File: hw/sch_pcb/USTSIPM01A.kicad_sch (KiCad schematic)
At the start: 41 parts, among them J4 HEADER_2x01_PARALLEL, J5 HEADER_2x01_PARALLEL, J6 HEADER_2x01_PARALLEL, J8 HEADER_2x01_PARALLEL, J9 HEADER_2x01_PARALLEL, M1 HOLE, M2 HOLE, M3 HOLE, M4 HOLE, U1 MICROFC-60035-SMT-TR(1), U2 OPA836IDB

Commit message: Edit schema
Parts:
- removed C1: 15uF/35V, Mlab_C:TantalC_SizeC_Reflow, symbol AIRDOSC01A_PCB01A-rescue:CP-Device
- added C1: 10uF/35V, Capacitor_SMD:C_0805_2012Metric, symbol Device:C
- C10, C11, C12, C13, C2: renamed from C?; footprint Mlab_R:SMD-0805 -> Capacitor_SMD:C_0805_2012Metric
- C3: UST_ID 5c70984412875079b91f8867 -> (none)
- C4, C7: value 10u -> 10uF; footprint Mlab_R:SMD-0805 -> Capacitor_SMD:C_0805_2012Metric; UST_ID 5c70984712875079b91f8b53 -> (none)
- C5, C6, C8, C9: footprint Mlab_R:SMD-0805 -> Capacitor_SMD:C_0805_2012Metric
- gave numbers to parts that had none: 6
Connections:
- net GND: now also C1.2
- net at R1.1, R2.2: now also C1.1
- net #PD: no longer names the net of R11.2, U2.5 (~{DIS})

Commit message: Editing schema and PCB
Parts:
- removed C3: 47uF, Mlab_C:TantalC_SizeC_Reflow, symbol AIRDOSC01A_PCB01A-rescue:CP-Device
- removed D1: M4, Mlab_D:Diode-SMA_Standard, symbol Device:D
- added C14, C15, C3: 10uF, Capacitor_SMD:C_0805_2012Metric, symbol Device:C
- added D1: BZX585-B5V6.115, Diode_SMD:D_SOD-523, symbol MLAB_D:D_ZENER
- L1: value 400uH cca 0,9mA -> 400uH cca 0,9mA NLV10JT391; footprint (none) -> Inductor_SMD:L_1210_3225Metric_Pad1.42x2.65mm_HandSolder
- R1, R10, R11, R12, R13, R2, R3, R4, R5, R6, R7, R8, R9: footprint Mlab_R:SMD-0805 -> Resistor_SMD:R_0805_2012Metric
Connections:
- net +3V6: now also C14.1, C15.1, C3.1, D1.1 (K)
- net GND: now also C14.2, C15.2, C3.2, D1.2 (A)
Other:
- moved on the sheet: C4, C7, C8, R3

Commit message: Editing PCB
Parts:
- removed M1, M2, M3, M4: HOLE, Mlab_Mechanical:MountingHole_3mm, symbol MLAB_MECHANICAL:HOLE
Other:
- note removed: "MOUNTING HOLES"
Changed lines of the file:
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@@
   (junction (at 121.412 127.508) (diameter 1.016) (color 0 0 0 0)
   )
-  (junction (at 269.24 15.24) (diameter 1.016) (color 0 0 0 0)
-  )
   (junction (at 60.452 100.838) (diameter 1.016) (color 0 0 0 0)
   )
-  (junction (at 264.16 15.24) (diameter 1.016) (color 0 0 0 0)
-  )
   (junction (at 144.78 53.848) (diameter 0) (color 0 0 0 0)
   )
@@
   )
   (junction (at 71.882 100.838) (diameter 1.016) (color 0 0 0 0)
-  )
-  (junction (at 274.32 15.24) (diameter 1.016) (color 0 0 0 0)
   )
   (no_connect (at 103.632 113.538))
@@
     (stroke (width 0) (type default) (color 0 0 0 0))
   )
-  (wire (pts (xy 279.4 15.24) (xy 279.4 16.51))
-    (stroke (width 0) (type solid) (color 0 0 0 0))
-  )
-  (wire (pts (xy 274.32 15.24) (xy 279.4 15.24))
-    (stroke (width 0) (type solid) (color 0 0 0 0))
-  )
-  (polyline (pts (xy 246.38 13.97) (xy 246.38 24.13))
-    (stroke (width 0) (type dash) (color 0 0 0 0))
-  )
   (wire (pts (xy 85.852 178.562) (xy 78.232 178.562))
     (stroke (width 0) (type solid) (color 0 0 0 0))
@@
     (stroke (width 0) (type solid) (color 0 0 0 0))
   )
-  (wire (pts (xy 269.24 15.24) (xy 274.32 15.24))
-    (stroke (width 0) (type solid) (color 0 0 0 0))
-  )
   (wire (pts (xy 144.272 147.828) (xy 155.702 147.828))
     (stroke (width 0) (type solid) (color 0 0 0 0))
@@
     (stroke (width 0) (type solid) (color 0 0 0 0))
   )
-  (polyline (pts (xy 281.94 13.97) (xy 281.94 24.13))
-    (stroke (width 0) (type dash) (color 0 0 0 0))
-  )
   (wire (pts (xy 60.452 112.268) (xy 60.452 110.998))
     (stroke (width 0) (type solid) (color 0 0 0 0))
@@
     (stroke (width 0) (type default) (color 0 0 0 0))
   )
-  (polyline (pts (xy 246.38 13.97) (xy 281.94 13.97))
-    (stroke (width 0) (type dash) (color 0 0 0 0))
-  )
-  (wire (pts (xy 264.16 15.24) (xy 269.24 15.24))
-    (stroke (width 0) (type solid) (color 0 0 0 0))
-  )
   (wire (pts (xy 46.482 100.838) (xy 49.022 100.838))
     (stroke (width 0) (type solid) (color 0 0 0 0))
   )
-  (wire (pts (xy 274.32 16.51) (xy 274.32 15.24))
-    (stroke (width 0) (type solid) (color 0 0 0 0))
-  )
   (wire (pts (xy 58.166 178.562) (xy 68.072 178.562))
     (stroke (width 0) (type solid) (color 0 0 0 0))
   )
-  (wire (pts (xy 259.08 16.51) (xy 259.08 15.24))
-    (stroke (width 0) (type solid) (color 0 0 0 0))
-  )
   (wire (pts (xy 144.78 64.008) (xy 148.59 64.008))
     (stroke (width 0) (type default) (color 0 0 0 0))
@@
     (stroke (width 0) (type solid) (color 0 0 0 0))
   )
-  (polyline (pts (xy 246.38 24.13) (xy 281.94 24.13))
-    (stroke (width 0) (type dash) (color 0 0 0 0))
-  )
   (wire (pts (xy 238.76 66.548) (xy 238.76 64.008))
     (stroke (width 0) (type default) (color 0 0 0 0))
@@
     (stroke (width 0) (type default) (color 0 0 0 0))
   )
-  (wire (pts (xy 259.08 15.24) (xy 264.16 15.24))
-    (stroke (width 0) (type solid) (color 0 0 0 0))
-  )
   (wire (pts (xy 195.58 56.388) (xy 195.58 53.848))
     (stroke (width 0) (type default) (color 0 0 0 0))
@@
     (stroke (width 0) (type solid) (color 0 0 0 0))
   )
-  (wire (pts (xy 269.24 16.51) (xy 269.24 15.24))
-    (stroke (width 0) (type solid) (color 0 0 0 0))
-  )
   (wire (pts (xy 58.166 189.992) (xy 58.166 187.452))
     (stroke (width 0) (type solid) (color 0 0 0 0))
@@
   )
   (wire (pts (xy 68.072 189.992) (xy 68.072 187.452))
-    (stroke (width 0) (type solid) (color 0 0 0 0))
-  )
-  (wire (pts (xy 264.16 16.51) (xy 264.16 15.24))
     (stroke (width 0) (type solid) (color 0 0 0 0))
   )
@@
   )
   (text "R2=R3*((Vout/1,25)-1)" (at 227.33 97.028 0)
-    (effects (font (size 1.524 1.524)) (justify left bottom))
-  )
-  (text "MOUNTING HOLES" (at 256.54 24.13 0)
     (effects (font (size 1.524 1.524)) (justify left bottom))
   )
@@
     )
   )
-  (symbol (lib_id "MLAB_MECHANICAL:HOLE") (at 259.08 17.78 90) (unit 1)
-    (in_bom yes) (on_board yes)
-    (property "Reference" "M1" (id 0) (at 259.08 20.32 90)
-      (effects (font (size 1.524 1.524)))
-    )
-    (property "Value" "HOLE" (id 1) (at 261.62 17.78 0)
-      (effects (font (size 1.524 1.524)) hide)
-    )
-    (property "Footprint" "Mlab_Mechanical:MountingHole_3mm" (id 2) (at 259.08 17.78 0)
-      (effects (font (size 1.524 1.524)) hide)
-    )
-    (property "Datasheet" "" (id 3) (at 259.08 17.78 0)
-      (effects (font (size 1.524 1.524)))
-    )
-    (pin "1")
-  )
-  (symbol (lib_id "MLAB_MECHANICAL:HOLE") (at 274.32 17.78 90) (unit 1)
-    (in_bom yes) (on_board yes)
-    (property "Reference" "M4" (id 0) (at 274.32 20.32 90)
-      (effects (font (size 1.524 1.524)))
-    )
-    (property "Value" "HOLE" (id 1) (at 276.86 17.78 0)
-      (effects (font (size 1.524 1.524)) hide)
-    )
-    (property "Footprint" "Mlab_Mechanical:MountingHole_3mm" (id 2) (at 274.32 17.78 0)
-      (effects (font (size 1.524 1.524)) hide)
-    )
-    (property "Datasheet" "" (id 3) (at 274.32 17.78 0)
-      (effects (font (size 1.524 1.524)))
-    )
-    (pin "1")
-  )
-  (symbol (lib_id "power:GND") (at 279.4 16.51 0) (unit 1)
-    (in_bom yes) (on_board yes)
-    (property "Reference" "#PWR023" (id 0) (at 279.4 22.86 0)
-      (effects (font (size 1.27 1.27)) hide)
-    )
-    (property "Value" "GND" (id 1) (at 279.527 20.9042 0))
-    (property "Footprint" "" (id 2) (at 279.4 16.51 0)
-      (effects (font (size 1.27 1.27)) hide)
-    )
-    (property "Datasheet" "" (id 3) (at 279.4 16.51 0)
-      (effects (font (size 1.27 1.27)) hide)
-    )
-    (pin "1")
-  )
   (symbol (lib_id "MLAB_IO:MICROFC-60035-SMT-TR(1)") (at 92.202 116.078 0) (mirror x) (unit 1)
     (in_bom yes) (on_board yes)
@@
     (property "Datasheet" "" (id 3) (at 71.882 112.268 0)
       (effects (font (size 1.27 1.27)) hide)
-    )
-    (pin "1")
-  )
-  (symbol (lib_id "MLAB_MECHANICAL:HOLE") (at 269.24 17.78 90) (unit 1)
-    (in_bom yes) (on_board yes)
-    (property "Reference" "M3" (id 0) (at 269.24 20.32 90)
-      (effects (font (size 1.524 1.524)))
-    )
-    (property "Value" "HOLE" (id 1) (at 271.78 17.78 0)
-      (effects (font (size 1.524 1.524)) hide)
-    )
-    (property "Footprint" "Mlab_Mechanical:MountingHole_3mm" (id 2) (at 269.24 17.78 0)
-      (effects (font (size 1.524 1.524)) hide)
-    )
-    (property "Datasheet" "" (id 3) (at 269.24 17.78 0)
-      (effects (font (size 1.524 1.524)))
-    )
-    (pin "1")
-  )
-  (symbol (lib_id "MLAB_MECHANICAL:HOLE") (at 264.16 17.78 90) (unit 1)
-    (in_bom yes) (on_board yes)
-    (property "Reference" "M2" (id 0) (at 264.16 20.32 90)
-      (effects (font (size 1.524 1.524)))
-    )
-    (property "Value" "HOLE" (id 1) (at 266.7 17.78 0)
-      (effects (font (size 1.524 1.524)) hide)
-    )
-    (property "Footprint" "Mlab_Mechanical:MountingHole_3mm" (id 2) (at 264.16 17.78 0)
-      (effects (font (size 1.524 1.524)) hide)
-    )
-    (property "Datasheet" "" (id 3) (at 264.16 17.78 0)
-      (effects (font (size 1.524 1.524)))
     )
     (pin "1")
@@
       (reference "#PWR022") (unit 1) (value "GND") (footprint "")
     )
-    (path "/00000000-0000-0000-0000-00005bac7ddd"
-      (reference "#PWR023") (unit 1) (value "GND") (footprint "")
-    )
     (path "/7ed9e500-4bce-4c8d-8ac2-1c6206b17017"
       (reference "#PWR024") (unit 1) (value "GND") (footprint "")
@@
       (reference "L1") (unit 1) (value "400uH cca 0,9mA NLV10JT391") (footprint "Inductor_SMD:L_1210_3225Metric_Pad1.42x2.65mm_HandSolder")
     )
-    (path "/00000000-0000-0000-0000-0000549d7549"
-      (reference "M1") (unit 1) (value "HOLE") (footprint "Mlab_Mechanical:MountingHole_3mm")
-    )
-    (path "/00000000-0000-0000-0000-00005c6d1882"
-      (reference "M2") (unit 1) (value "HOLE") (footprint "Mlab_Mechanical:MountingHole_3mm")
-    )
-    (path "/00000000-0000-0000-0000-00005c6d1820"
-      (reference "M3") (unit 1) (value "HOLE") (footprint "Mlab_Mechanical:MountingHole_3mm")
-    )
-    (path "/00000000-0000-0000-0000-0000549d7665"
-      (reference "M4") (unit 1) (value "HOLE") (footprint "Mlab_Mechanical:MountingHole_3mm")
-    )
     (path "/00000000-0000-0000-0000-00005c6c24df"

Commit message: Priprava vyrobnich dat
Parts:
- C1: value 10uF/35V -> (none); footprint Capacitor_SMD:C_0805_2012Metric -> (none); UST_ID (none) -> 628d183cdc56076e9a223682
- C10, C13: value 1uF/50V -> (none); footprint Capacitor_SMD:C_0805_2012Metric -> (none); UST_ID (none) -> 5c70984712875079b91f8b6f
- C11, C12: value 100nF -> (none); footprint Capacitor_SMD:C_0805_2012Metric -> (none); UST_ID (none) -> 5c70984712875079b91f8b4c
- C14, C15, C2, C3, C4, C7: value 10uF -> (none); footprint Capacitor_SMD:C_0805_2012Metric -> (none); UST_ID (none) -> 5c70984712875079b91f8b53
- C5, C6, C8: value 100nF -> (none); footprint Capacitor_SMD:C_0805_2012Metric -> (none)
- C50: renamed from R8; value 100nF -> (none); footprint Resistor_SMD:R_0805_2012Metric -> (none)
- C9: value 10nF -> (none); footprint Capacitor_SMD:C_0805_2012Metric -> (none)
- D1: value BZX585-B5V6.115 -> (none); footprint Diode_SMD:D_SOD-523 -> (none)
- D2: value NSR05T40XV2T5G -> (none); footprint Diode_SMD:D_SOD-523 -> (none); UST_ID (none) -> 5c70984712875079b91f8b7b
- J4, J5, J6, J8, J9: value HEADER_2x01_PARALLEL -> (none); footprint Mlab_Pin_Headers:Straight_2x01 -> (none)
- L1: value 400uH cca 0,9mA NLV10JT391 -> (none); footprint Inductor_SMD:L_1210_3225Metric_Pad1.42x2.65mm_HandSolder -> (none); UST_ID (none) -> 628d18f5dc56076e9a2236a9
- R1, R13: value 100R -> (none); footprint Resistor_SMD:R_0805_2012Metric -> (none); UST_ID (none) -> 5c70984512875079b91f8977
- R10: value 12k -> (none); footprint Resistor_SMD:R_0805_2012Metric -> (none)
- R11: value 10k -> (none); footprint Resistor_SMD:R_0805_2012Metric -> (none); UST_ID (none) -> 5c70984612875079b91f899f
- R12: value 1k -> (none); footprint Resistor_SMD:R_0805_2012Metric -> (none)
- R2, R4, R5: value 10R -> (none); footprint Resistor_SMD:R_0805_2012Metric -> (none)
- R3: value 100R -> (none); footprint Resistor_SMD:R_0805_2012Metric -> (none)
- R6: value 3M9 -> (none); footprint Resistor_SMD:R_0805_2012Metric -> (none); UST_ID (none) -> 628d19cddc56076e9a2236db
- R7: value 160k -> (none); footprint Resistor_SMD:R_0805_2012Metric -> (none); UST_ID (none) -> 628d19e8dc56076e9a2236eb
- R9: value 470R -> (none); footprint Resistor_SMD:R_0805_2012Metric -> (none)
- U1: value MICROFC-60035-SMT-TR(1) -> (none); footprint Mlab_IO:MicroFC−60035−SMT -> (none)
- U2: value OPA836IDB -> (none); footprint Package_TO_SOT_SMD:SOT-23-6 -> (none)
- U3: value MAX5026 -> (none); footprint Package_TO_SOT_SMD:SOT-23-6_Handsoldering -> (none); UST_ID (none) -> 5c70984712875079b91f8b7c

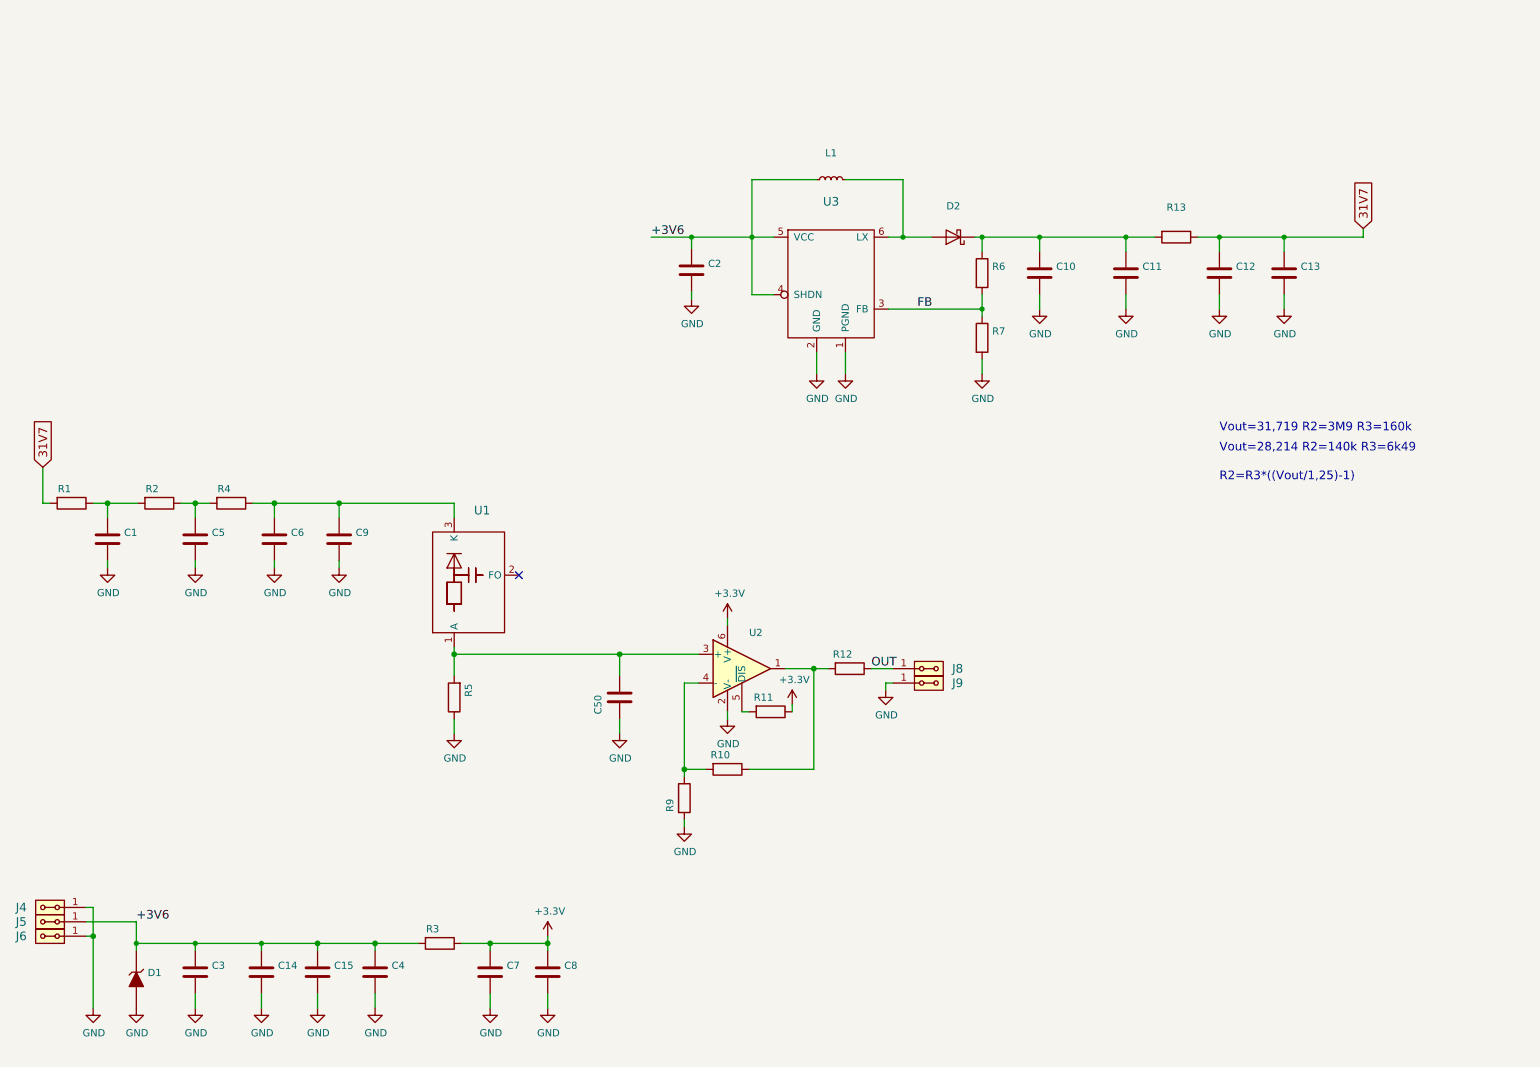
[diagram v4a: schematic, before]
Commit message: Edit UST ID for 3M9
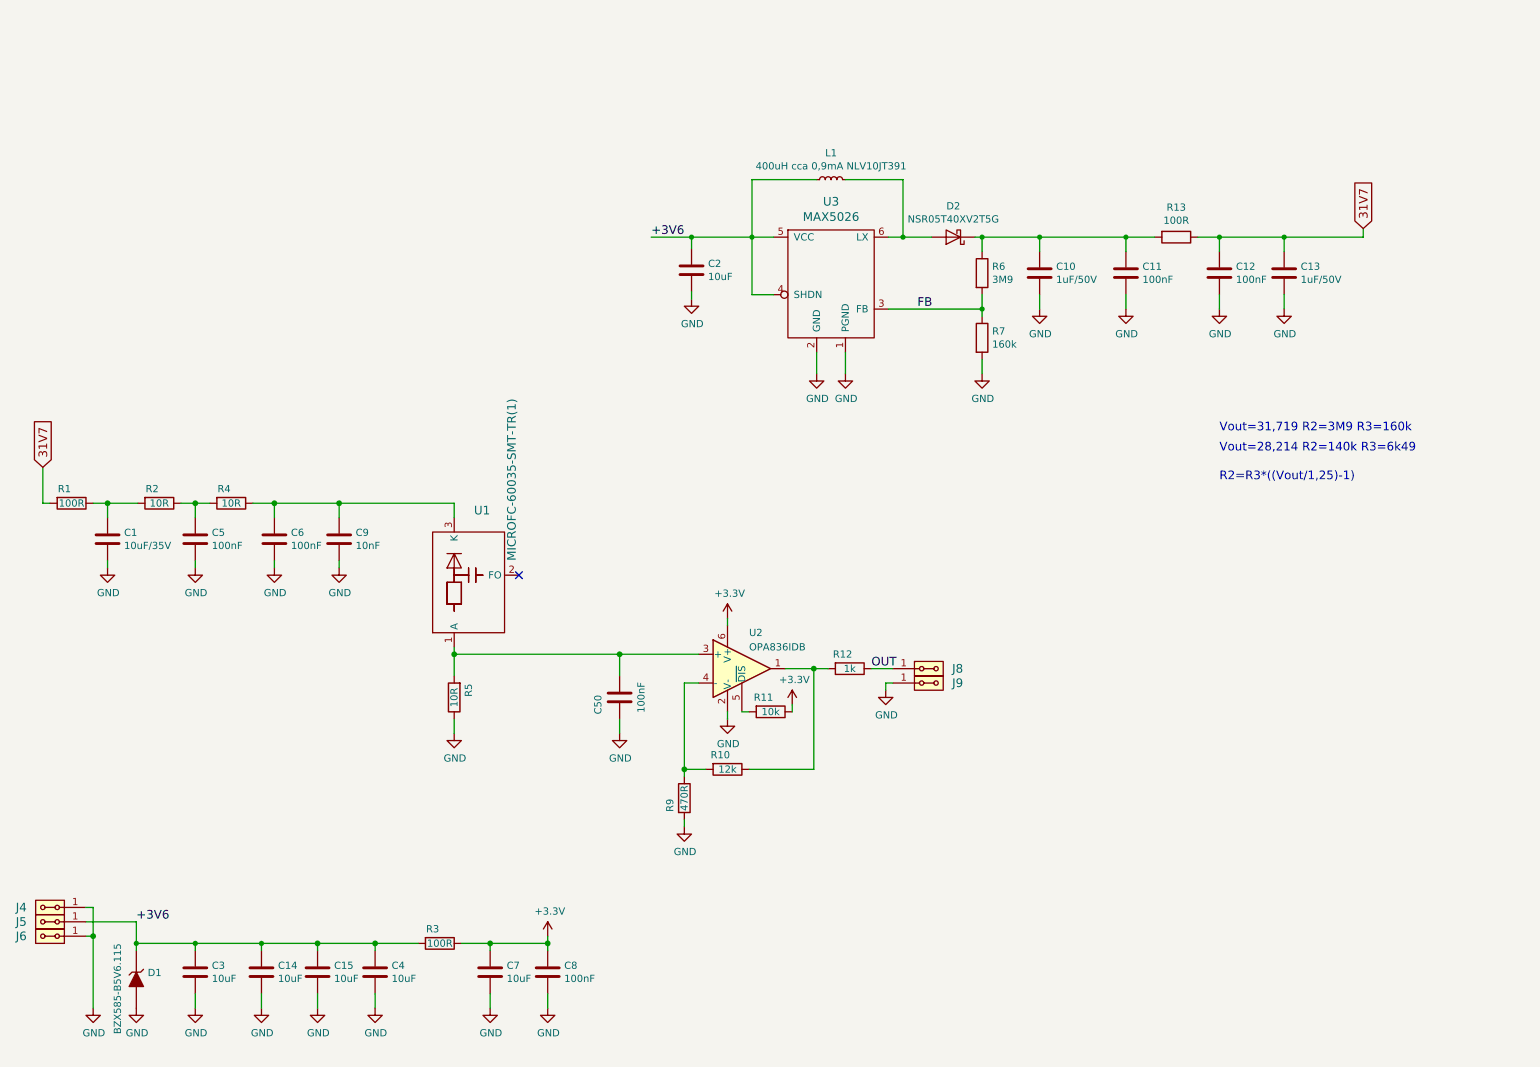
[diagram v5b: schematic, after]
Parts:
- C1: value (none) -> 10uF/35V; footprint (none) -> Capacitor_SMD:C_0805_2012Metric
- C10, C13: value (none) -> 1uF/50V; footprint (none) -> Capacitor_SMD:C_0805_2012Metric
- C11, C12, C5, C50, C6, C8: value (none) -> 100nF; footprint (none) -> Capacitor_SMD:C_0805_2012Metric
- C14, C15, C2, C3, C4, C7: value (none) -> 10uF; footprint (none) -> Capacitor_SMD:C_0805_2012Metric
- C9: value (none) -> 10nF; footprint (none) -> Capacitor_SMD:C_0805_2012Metric
- D1: value (none) -> BZX585-B5V6.115; footprint (none) -> Diode_SMD:D_SOD-523
- D2: value (none) -> NSR05T40XV2T5G; footprint (none) -> Diode_SMD:D_SOD-523
- J4, J5, J6, J8, J9: value (none) -> HEADER_2x01_PARALLEL; footprint (none) -> Mlab_Pin_Headers:Straight_2x01
- L1: value (none) -> 400uH cca 0,9mA NLV10JT391; footprint (none) -> Inductor_SMD:L_1210_3225Metric_Pad1.42x2.65mm_HandSolder
- R1, R13, R3: value (none) -> 100R; footprint (none) -> Resistor_SMD:R_0805_2012Metric
- R10: value (none) -> 12k; footprint (none) -> Resistor_SMD:R_0805_2012Metric
- R11: value (none) -> 10k; footprint (none) -> Resistor_SMD:R_0805_2012Metric
- R12: value (none) -> 1k; footprint (none) -> Resistor_SMD:R_0805_2012Metric
- R2, R4, R5: value (none) -> 10R; footprint (none) -> Resistor_SMD:R_0805_2012Metric
- R6: value (none) -> 3M9; footprint (none) -> Resistor_SMD:R_0805_2012Metric; UST_ID 628d19cddc56076e9a2236db -> 62c7d4f48c8e243169d1938e
- R7: value (none) -> 160k; footprint (none) -> Resistor_SMD:R_0805_2012Metric
- R9: value (none) -> 470R; footprint (none) -> Resistor_SMD:R_0805_2012Metric
- U1: value (none) -> MICROFC-60035-SMT-TR(1); footprint (none) -> Mlab_IO:MicroFC−60035−SMT
- U2: value (none) -> OPA836IDB; footprint (none) -> Package_TO_SOT_SMD:SOT-23-6
- U3: value (none) -> MAX5026; footprint (none) -> Package_TO_SOT_SMD:SOT-23-6_Handsoldering
